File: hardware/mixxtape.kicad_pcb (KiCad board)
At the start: 2 copper layers, 100.3 x 63.5 mm, 0 parts

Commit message: hardware: enforce the 5,000-stock supply-chain rule; case-fit test sheet
Steven's rule: every fitted part needs 5,000+ in stock at JLCPCB, and a
common part beats a capable one — a run of 20 hand-built boards is not
worth a redesign because a clever chip went end-of-life. gen_bom.py now
enforces it and prints a rule section; find_common_parts.py searches for
compliant alternatives.

Audit result: everything clears the bar except the microphone.

That exception is worth stating plainly. No digital MEMS microphone at
JLCPCB meets the rule — the category is thin and the best-stocked digital
part is about 3.5k. The one microphone that does clear 5,000 (ZTS6216,
C481302, 29k) is analog: it wants a DC-blocking cap and a gain stage into
the ESP32's ADC, which the brief already describes as a lo-fi path with
roughly nine effective bits. Following the rule there would satisfy the
letter of it and destroy the product's only input, so the BOM records a
digital part at ~3.5k as an accepted exception with three qualified
alternates. 20 pieces against 3.5k stock is 174x coverage.

The specified mic (C2840615) is still at zero stock and is deliberately
NOT swapped in the schematic yet, because the replacement's footprint and
port direction have not been confirmed and this design needs a
bottom-ported part.

Also adds the case-fit test: a 1:1 printable outline with a 50 mm
calibration bar, since printers scale pages without saying so and a
scaled sheet would make the whole test lie. Plus a pre-production
checklist covering the fit test, the open decisions, what to re-quote,
and the three prototype questions that could still change the hardware.

Co-Authored-By: Claude Opus 5 <noreply@anthropic.com>
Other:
- board text added: "50.0 mm"
- board text added: "If it is not exactly 50.0 mm, the printer scaled the page and"
- board text added: "MEASURE THIS BAR FIRST."
- board text added: "actual size, with any fit-to-page option turned off."
- board text added: "nothing else on this sheet can be trusted. Reprint at 100% /"
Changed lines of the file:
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@@
 		(stroke (width 0.12) (type solid)) (layer "F.SilkS")
+	)
+	(gr_line (start 142.000 37.500) (end 192.000 37.500)
+		(stroke (width 0.25) (type solid)) (layer "Dwgs.User")
+	)
+	(gr_line (start 142.000 37.500) (end 142.000 35.000)
+		(stroke (width 0.25) (type solid)) (layer "Dwgs.User")
+	)
+	(gr_line (start 147.000 37.500) (end 147.000 36.300)
+		(stroke (width 0.25) (type solid)) (layer "Dwgs.User")
+	)
+	(gr_line (start 152.000 37.500) (end 152.000 36.300)
+		(stroke (width 0.25) (type solid)) (layer "Dwgs.User")
+	)
+	(gr_line (start 157.000 37.500) (end 157.000 36.300)
+		(stroke (width 0.25) (type solid)) (layer "Dwgs.User")
+	)
+	(gr_line (start 162.000 37.500) (end 162.000 36.300)
+		(stroke (width 0.25) (type solid)) (layer "Dwgs.User")
+	)
+	(gr_line (start 167.000 37.500) (end 167.000 35.000)
+		(stroke (width 0.25) (type solid)) (layer "Dwgs.User")
+	)
+	(gr_line (start 172.000 37.500) (end 172.000 36.300)
+		(stroke (width 0.25) (type solid)) (layer "Dwgs.User")
+	)
+	(gr_line (start 177.000 37.500) (end 177.000 36.300)
+		(stroke (width 0.25) (type solid)) (layer "Dwgs.User")
+	)
+	(gr_line (start 182.000 37.500) (end 182.000 36.300)
+		(stroke (width 0.25) (type solid)) (layer "Dwgs.User")
+	)
+	(gr_line (start 187.000 37.500) (end 187.000 36.300)
+		(stroke (width 0.25) (type solid)) (layer "Dwgs.User")
+	)
+	(gr_line (start 192.000 37.500) (end 192.000 35.000)
+		(stroke (width 0.25) (type solid)) (layer "Dwgs.User")
+	)
+	(gr_text "50.0 mm" (at 142.000 32.500 0) (layer "Dwgs.User")
+		(effects (font (size 1.6 1.6) (thickness 0.2)) (justify left))
+	)
+	(gr_text "MEASURE THIS BAR FIRST." (at 142.000 41.000 0) (layer "Dwgs.User")
+		(effects (font (size 1.1 1.1) (thickness 0.2)) (justify left))
+	)
+	(gr_text "If it is not exactly 50.0 mm, the printer scaled the page and" (at 142.000 43.400 0) (layer "Dwgs.User")
+		(effects (font (size 1.1 1.1) (thickness 0.2)) (justify left))
+	)
+	(gr_text "nothing else on this sheet can be trusted. Reprint at 100% /" (at 142.000 45.800 0) (layer "Dwgs.User")
+		(effects (font (size 1.1 1.1) (thickness 0.2)) (justify left))
+	)
+	(gr_text "actual size, with any fit-to-page option turned off." (at 142.000 48.200 0) (layer "Dwgs.User")
+		(effects (font (size 1.1 1.1) (thickness 0.2)) (justify left))
 	)
 	(gr_text "MECHANICAL ONLY - no components placed, no routing." (at 34.000 102.500 0) (layer "Cmts.User")

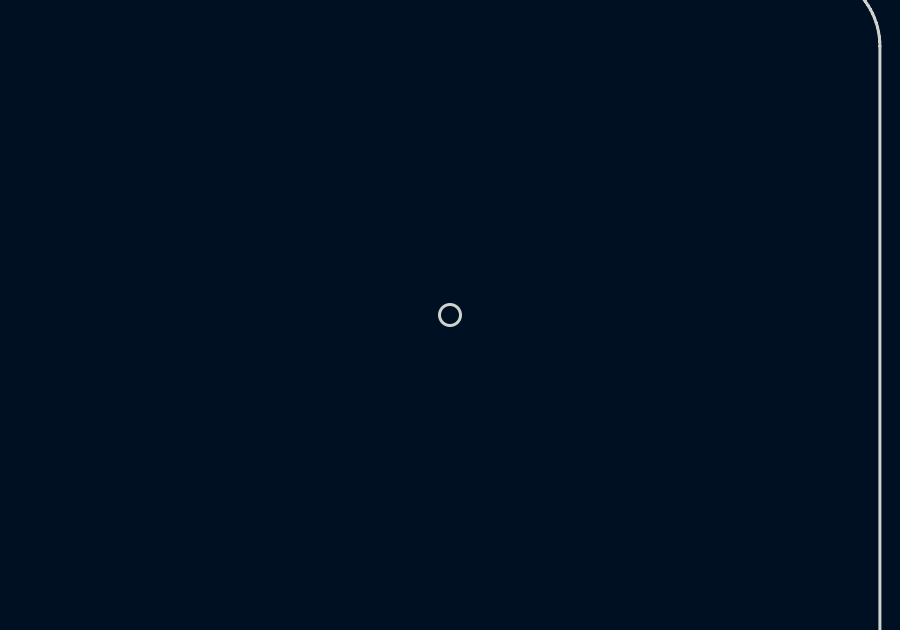
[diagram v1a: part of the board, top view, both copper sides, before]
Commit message: hardware: mic datasheet review — the brief's "bottom-ported" is wrong
Read the datasheets before committing to a replacement microphone, and
the more important finding was about the part we already had.

The brief specifies MSM261S4030H0R as bottom-ported and calls for a
0.5-0.8 mm acoustic hole through the board beneath it. Its datasheet says
otherwise on page 2: "omnidirectional, Top-ported, I2S digital output".
Every in-stock alternative in that family is top-ported too. Sound enters
from the component side, so that hole would have done nothing but weaken
the board and give a false sense the acoustics were handled. Removed from
the mechanical layout, replaced with a keep-clear annotation, and the
brief corrected at source since other agents are told to follow it.

On the replacement itself, MSM261DHT006 (C51928215) is an equal swap
rather than a downgrade: identical -26 dBFS sensitivity, same 1.6-3.6 V
range, same 4x3 mm LGA-8 footprint, 1 dB less SNR (60 vs 61) and 2 dB
better acoustic overload (122 vs 120 dB SPL), which is the more useful
end for a recorder that will meet a door slam. It is also cheaper and
draws less.

Its one real cost is the interface: PDM instead of I2S. That is a
firmware change - the ESP32 reads PDM in hardware - not a board change.

If avoiding that is worth money, ICS-43434 keeps I2S and gains 5 dB of
SNR on the riskiest subsystem in the project, at 7x the price and a
different footprint.

Co-Authored-By: Claude Opus 5 <noreply@anthropic.com>
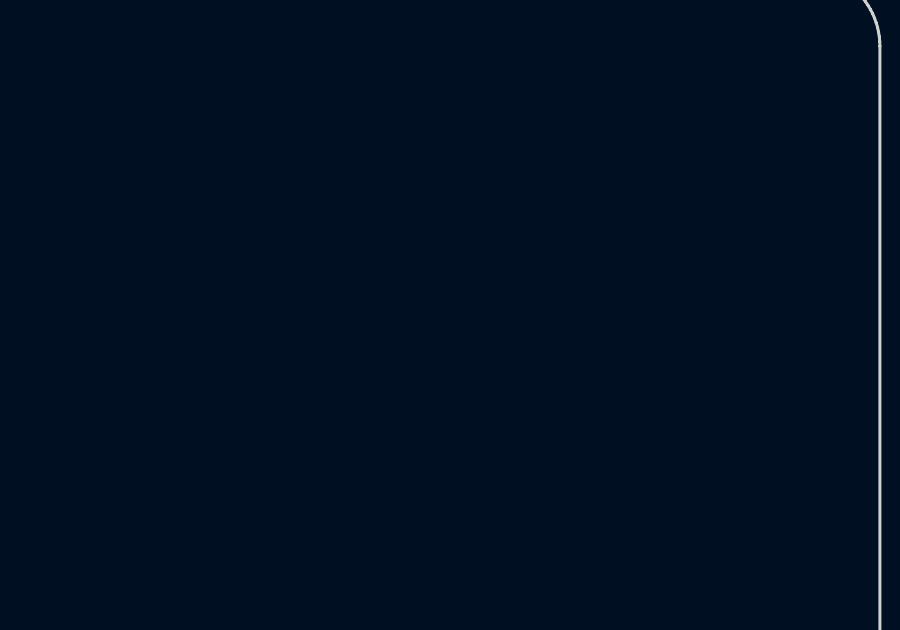
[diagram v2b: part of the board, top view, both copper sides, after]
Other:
- outline, holes or cut-outs redrawn
- board text added: "CORRECTION: the brief specifies an acoustic hole through the"
- board text added: "board for a bottom-ported mic. The specified part and every"
- board text added: "in-stock alternative are TOP-ported, so no hole is drawn. Keep"
- board text added: "mic faces UP - keep clear, no hole needed"
- board text added: "the mic's top face clear of ribs, labels and fingers instead."
- board text removed: "mic port — keep clear"
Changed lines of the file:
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@@
 		(stroke (width 0.1) (type solid)) (fill no) (layer "Edge.Cuts")
 	)
-	(gr_circle (center 116.000 41.500) (end 116.350 41.500)
-		(stroke (width 0.1) (type solid)) (fill no) (layer "Edge.Cuts")
+	(gr_circle (center 116.000 41.500) (end 118.000 41.500)
+		(stroke (width 0.15) (type solid)) (fill no) (layer "Dwgs.User")
 	)
-	(gr_circle (center 116.000 41.500) (end 117.200 41.500)
-		(stroke (width 0.1) (type solid)) (fill no) (layer "Dwgs.User")
-	)
-	(gr_text "mic port — keep clear" (at 106.000 44.500 0) (layer "Cmts.User")
+	(gr_text "mic faces UP - keep clear, no hole needed" (at 96.000 45.000 0) (layer "Cmts.User")
 		(effects (font (size 0.9 0.9) (thickness 0.2)) (justify left))
 	)
@@
 		(effects (font (size 1.0 1.0) (thickness 0.2)) (justify left))
 	)
-	(gr_text "DEFERRED: the five decorative guide holes along the bottom edge." (at 34.000 128.900 0) (layer "Cmts.User")
+	(gr_text "CORRECTION: the brief specifies an acoustic hole through the" (at 34.000 128.900 0) (layer "Cmts.User")
 		(effects (font (size 1.0 1.0) (thickness 0.2)) (justify left))
 	)
-	(gr_text "They never enter a deck, so they are artwork rather than" (at 34.000 131.100 0) (layer "Cmts.User")
+	(gr_text "board for a bottom-ported mic. The specified part and every" (at 34.000 131.100 0) (layer "Cmts.User")
 		(effects (font (size 1.0 1.0) (thickness 0.2)) (justify left))
 	)
-	(gr_text "mechanism, and guessed positions would constrain placement for" (at 34.000 133.300 0) (layer "Cmts.User")
+	(gr_text "in-stock alternative are TOP-ported, so no hole is drawn. Keep" (at 34.000 133.300 0) (layer "Cmts.User")
 		(effects (font (size 1.0 1.0) (thickness 0.2)) (justify left))
 	)
-	(gr_text "no reason. Add them with the silkscreen artwork." (at 34.000 135.500 0) (layer "Cmts.User")
+	(gr_text "the mic's top face clear of ribs, labels and fingers instead." (at 34.000 135.500 0) (layer "Cmts.User")
 		(effects (font (size 1.0 1.0) (thickness 0.2)) (justify left))
 	)
+	(gr_text "" (at 34.000 137.700 0) (layer "Cmts.User")
+		(effects (font (size 1.0 1.0) (thickness 0.2)) (justify left))
+	)
+	(gr_text "DEFERRED: the five decorative guide holes along the bottom edge." (at 34.000 139.900 0) (layer "Cmts.User")
+		(effects (font (size 1.0 1.0) (thickness 0.2)) (justify left))
+	)
+	(gr_text "They never enter a deck, so they are artwork rather than" (at 34.000 142.100 0) (layer "Cmts.User")
+		(effects (font (size 1.0 1.0) (thickness 0.2)) (justify left))
+	)
+	(gr_text "mechanism, and guessed positions would constrain placement for" (at 34.000 144.300 0) (layer "Cmts.User")
+		(effects (font (size 1.0 1.0) (thickness 0.2)) (justify left))
+	)
+	(gr_text "no reason. Add them with the silkscreen artwork." (at 34.000 146.500 0) (layer "Cmts.User")
+		(effects (font (size 1.0 1.0) (thickness 0.2)) (justify left))
+	)
